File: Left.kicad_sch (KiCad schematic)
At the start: 193 parts, among them J1 USB_C_Receptacle_USB2.0, J2 USB_C_Receptacle_USB2.0, J3 AVR-ISP-6, Q1 DMN2041L, Q2 DMN2041L, SW1 RotaryEncoder, SW10 SW_Push, SW11 SW_Push, SW12 SW_Push, SW13 SW_Push, SW14 SW_Push, SW15 SW_Push, SW16 SW_Push, SW17 SW_Push, SW18 SW_Push, SW19 SW_Push, SW2 SW_Push, SW20 SW_Push, SW21 SW_Push, SW22 SW_Push, SW23 SW_Push, SW24 SW_Push, SW25 SW_Push, SW26 SW_Push, SW27 SW_Push, SW28 SW_Push, SW29 SW_Push, SW3 SW_Push, SW30 SW_Push, SW31 SW_Push, SW32 SW_Push, SW33 SW_Push, SW34 SW_Push, SW35 SW_Push, SW36 SW_Push, SW37 SW_Push, SW38 SW_Push, SW39 SW_Push, SW4 SW_Push, SW40 SW_Push, SW41 SW_Push, SW5 SW_Push, SW6 SW_Push, SW7 SW_Push, SW8 SW_Push, SW9 SW_Push, U1 ATmega32U4-A, Y1 16MHz

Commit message: replaced LEDs with RGBs, and started the PCB for keyboard
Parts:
- removed D10, D11, D12, D13, D14, D15, D16, D17, D18, D19, D2, D20, D21, D22, D23, D24, D25, D26, D27, D28, D29, D3, D30, D31, D32, D33, D34, D35, D36, D37, D38, D39, D4, D40, D41, D5, D6, D7, D8, D9: LED, symbol Device:LED
- removed D42, D47, D48, D54, D55, D62, D63, D69, D70, D76, D77: D_Small, symbol Device:D_Small
- removed Q1: DMN2041L, Package_TO_SOT_SMD:SOT-23, symbol Transistor_FET:DMN2041L
- removed R10, R11, R12, R13, R14, R15, R16, R17, R19, R20, R21, R24, R25, R26, R27, R28, R29, R3, R30, R31, R32, R33, R34, R35, R37, R38, R39, R4, R42, R43, R44, R45, R46, R47, R48, R5, R6, R7, R8, R9: 470, symbol Device:R_Small
- removed R49: 1k, symbol Device:R_Small
- removed SW14, SW15, SW2, SW21, SW22, SW28, SW29, SW35, SW36, SW7, SW8: SW_Push, keyswitches.pretty-2:Kailh_socket_PG1350, symbol Switch:SW_Push
- added C208, C209, C210, C211, C212, C213, C214, C215, C216, C217, C218, C219, C220, C221, C222, C223, C224, C225, C226, C227, C228, C229, C230, C231, C232, C233, C234, C235, C236, C237, C238, C239, C240, C241, C242, C243, C244, C245, C246, C247: 100nF, Capacitor_SMD:C_0402_1005Metric, symbol Device:C_Small
- added D203, D204, D205, D206, D207, D208, D209, D210, D211, D212, D213, D214, D215, D216, D217, D218, D219, D220, D221, D222, D223, D224, D225, D226, D227, D228, D229, D230, D231, D232, D233, D234, D235, D236, D237, D238, D239, D240, D241, D242: NeoPixel_THT, kicad-keyboard-parts.pretty:LED_RGB_Wuerth-PLCC4_3.2x2.8mm_150141M173100, symbol LED:NeoPixel_THT
- added D273, D274, D275, D276, D277, D278, D279, D280, D281, D282: D_Small, Diode_SMD:D_SOD-123, symbol Device:D_Small
- added FB201: FerriteBead_Small, Inductor_SMD:L_0805_2012Metric_Pad1.15x1.40mm_HandSolder, symbol Device:FerriteBead_Small
- added H201, H202, H203, H204, H205, H206: MountingHole, MountingHole:MountingHole_2.2mm_M2_DIN965_Pad, symbol Mechanical:MountingHole
- added R205: 300, Resistor_SMD:R_0402_1005Metric, symbol Device:R_Small
- added SW232, SW233, SW234, SW235, SW237, SW238, SW239, SW240, SW241: SW_Push, keyswitches.pretty-2:Kailh_socket_PG1350, symbol Switch:SW_Push
- added SW236: SW_Push, keyswitches.pretty-2:Kailh_socket_PG1350_2.25U, symbol Switch:SW_Push
- C201: renamed from C1; footprint (none) -> Capacitor_SMD:C_0402_1005Metric
- C202: renamed from C2; footprint (none) -> Capacitor_SMD:C_0402_1005Metric
- C203: renamed from C3; footprint (none) -> Capacitor_SMD:C_0402_1005Metric
- C204: renamed from C4; footprint (none) -> Capacitor_SMD:C_0402_1005Metric
- C205: renamed from C5; footprint (none) -> Capacitor_SMD:C_0402_1005Metric
- C206: renamed from C6; footprint (none) -> Capacitor_SMD:C_0402_1005Metric
- C207: renamed from C7; footprint (none) -> Capacitor_SMD:C_0402_1005Metric
- D243: renamed from D43; footprint (none) -> Diode_SMD:D_SOD-123
- D244: renamed from D44; footprint (none) -> Diode_SMD:D_SOD-123
- D245: renamed from D45; footprint (none) -> Diode_SMD:D_SOD-123
- D246: renamed from D46; footprint (none) -> Diode_SMD:D_SOD-123
- D247: renamed from D49; footprint (none) -> Diode_SMD:D_SOD-123
- D248: renamed from D50; footprint (none) -> Diode_SMD:D_SOD-123
- D249: renamed from D51; footprint (none) -> Diode_SMD:D_SOD-123
- D250: renamed from D52; footprint (none) -> Diode_SMD:D_SOD-123
- D251: renamed from D53; footprint (none) -> Diode_SMD:D_SOD-123
- D252: renamed from D56; footprint (none) -> Diode_SMD:D_SOD-123
- D253: renamed from D57; footprint (none) -> Diode_SMD:D_SOD-123
- D254: renamed from D58; footprint (none) -> Diode_SMD:D_SOD-123
- D255: renamed from D59; footprint (none) -> Diode_SMD:D_SOD-123
- D256: renamed from D60; footprint (none) -> Diode_SMD:D_SOD-123
- D257: renamed from D64; footprint (none) -> Diode_SMD:D_SOD-123
- D258: renamed from D65; footprint (none) -> Diode_SMD:D_SOD-123
- D259: renamed from D66; footprint (none) -> Diode_SMD:D_SOD-123
- D260: renamed from D67; footprint (none) -> Diode_SMD:D_SOD-123
- D261: renamed from D68; footprint (none) -> Diode_SMD:D_SOD-123
- D262: renamed from D61; footprint (none) -> LED_SMD:LED_PLCC_2835
- D263: renamed from D71; footprint (none) -> Diode_SMD:D_SOD-123
- D264: renamed from D72; footprint (none) -> Diode_SMD:D_SOD-123
- D265: renamed from D73; footprint (none) -> Diode_SMD:D_SOD-123
- D266: renamed from D74; footprint (none) -> Diode_SMD:D_SOD-123
- D267: renamed from D75; footprint (none) -> Diode_SMD:D_SOD-123
- D268: renamed from D78; footprint (none) -> Diode_SMD:D_SOD-123
- D269: renamed from D79; footprint (none) -> Diode_SMD:D_SOD-123
- D270: renamed from D80; footprint (none) -> Diode_SMD:D_SOD-123
- D271: renamed from D81; footprint (none) -> Diode_SMD:D_SOD-123
- D272: renamed from D82; footprint (none) -> Diode_SMD:D_SOD-123
- F201: renamed from F1; footprint (none) -> Keebio-Parts:Fuse_0805
- J201: renamed from J2; footprint (none) -> Type-C:HRO-TYPE-C-31-M-13
- J202: renamed from J1; footprint (none) -> Type-C:HRO-TYPE-C-31-M-13
- J203: renamed from J3; footprint (none) -> Keebio-Parts:ICSP-Header
- R201: renamed from R1; footprint (none) -> Resistor_SMD:R_0402_1005Metric
- R202: renamed from R52; footprint (none) -> Resistor_SMD:R_0402_1005Metric
- R203: renamed from R2; footprint (none) -> Resistor_SMD:R_0402_1005Metric
- R204: renamed from R53; footprint (none) -> Resistor_SMD:R_0402_1005Metric
- R220: renamed from R18; footprint (none) -> Resistor_SMD:R_0402_1005Metric
- R224: renamed from R22; footprint (none) -> Resistor_SMD:R_0402_1005Metric
- R225: renamed from R23; footprint (none) -> Resistor_SMD:R_0402_1005Metric
- R238: renamed from R36; footprint (none) -> Resistor_SMD:R_0402_1005Metric
- R242: renamed from R40; footprint (none) -> Resistor_SMD:R_0402_1005Metric
- R243: renamed from R41; footprint (none) -> Resistor_SMD:R_0402_1005Metric
- R252: renamed from R50; footprint (none) -> Resistor_SMD:R_0402_1005Metric
- R253: renamed from R51; footprint (none) -> Resistor_SMD:R_0402_1005Metric
- SW202: renamed from SW1; footprint (none) -> Rotary_Encoder.pretty:kailh_EN97xx_rotary_encoder
- SW213: renamed from SW17; footprint keyswitches.pretty-2:Kailh_socket_PG1350 -> keyswitches.pretty-2:Kailh_socket_PG1350_1.5U
- SW214: renamed from SW18; footprint keyswitches.pretty-2:Kailh_socket_PG1350 -> keyswitches.pretty-2:Kailh_socket_PG1350_1.75U
- SW215: renamed from SW19; footprint keyswitches.pretty-2:Kailh_socket_PG1350 -> keyswitches.pretty-2:Kailh_socket_PG1350_2.25U
- SW216: renamed from SW20; footprint keyswitches.pretty-2:Kailh_socket_PG1350 -> keyswitches.pretty-2:Kailh_socket_PG1350_1.25U
- SW221: renamed from SW27; footprint keyswitches.pretty-2:Kailh_socket_PG1350 -> keyswitches.pretty-2:Kailh_socket_PG1350_1.25U
- SW226: renamed from SW34; footprint keyswitches.pretty-2:Kailh_socket_PG1350 -> keyswitches.pretty-2:Kailh_socket_PG1350_1.25U
- SW231: renamed from SW41; footprint keyswitches.pretty-2:Kailh_socket_PG1350 -> keyswitches.pretty-2:Kailh_socket_PG1350_1.25U
- Y201: renamed from Y1; footprint (none) -> Crystal:Crystal_SMD_3225-4Pin_3.2x2.5mm
- gave numbers to parts that had none: 1
- renumbered D1 to D201, Q2 to Q202, SW_RESET1 to SW201, SW3 to SW203, SW4 to SW204, SW5 to SW205, SW6 to SW206, SW9 to SW207, SW10 to SW208, SW11 to SW209, SW12 to SW210, SW13 to SW211, SW16 to SW212, SW23 to SW217, SW24 to SW218, SW25 to SW219, SW26 to SW220, SW30 to SW222, SW31 to SW223, SW32 to SW224, SW33 to SW225, SW37 to SW227, SW38 to SW228, SW39 to SW229, SW40 to SW230, U1 to U201
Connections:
- net +5V: now also C208.2, C209.2, C210.2, C211.2, C212.1, C212.2, C213.2, C214.2, C215.2, C216.2, C217.2, C218.2, C219.2, C220.2, C221.2, C222.2, C223.2, C224.2, C225.2, C226.2, C227.2, C228.2, C229.2, C230.2, C231.2, C232.2, C233.2, C234.2, C235.2, C236.2, C237.2, C238.2, C239.2, C240.2, C241.2, C242.2, C243.2, C244.2, C245.2, C246.2, C247.1, C247.2, D203.3 (VDD), D204.3 (VDD), D205.3 (VDD), D206.3 (VDD), D207.3 (VDD), D208.3 (VDD), D209.3 (VDD), D210.3 (VDD), D211.3 (VDD), D212.3 (VDD), D213.3 (VDD), D214.3 (VDD), D215.3 (VDD), D216.3 (VDD), D217.3 (VDD), D218.3 (VDD), D219.3 (VDD), D220.3 (VDD), D221.3 (VDD), D222.3 (VDD), D223.3 (VDD), D224.3 (VDD), D225.3 (VDD), D226.3 (VDD), D227.3 (VDD), D228.3 (VDD), D229.3 (VDD), D230.3 (VDD), D231.3 (VDD), D232.3 (VDD), D233.3 (VDD), D234.2 (GND), D234.3 (VDD), D235.3 (VDD), D236.3 (VDD), D237.3 (VDD), D238.3 (VDD), D239.3 (VDD), D240.3 (VDD), D241.3 (VDD), D242.3 (VDD)
- net GND: now also C208.1, C209.1, C210.1, C211.1, C213.1, C214.1, C215.1, C216.1, C217.1, C218.1, C219.1, C220.1, C221.1, C222.1, C223.1, C224.1, C225.1, C226.1, C227.1, C228.1, C229.1, C230.1, C231.1, C232.1, C233.1, C234.1, C235.1, C236.1, C237.1, C238.1, C239.1, C240.1, C241.1, C242.1, C243.1, C244.1, C245.1, C246.1, D203.2 (GND), D204.2 (GND), D205.2 (GND), D206.2 (GND), D207.2 (GND), D208.2 (GND), D209.2 (GND), D210.2 (GND), D211.2 (GND), D212.2 (GND), D213.2 (GND), D214.2 (GND), D215.2 (GND), D216.2 (GND), D217.2 (GND), D218.2 (GND), D219.2 (GND), D220.2 (GND), D221.2 (GND), D222.2 (GND), D223.2 (GND), D224.2 (GND), D225.2 (GND), D226.2 (GND), D227.2 (GND), D228.2 (GND), D229.2 (GND), D230.2 (GND), D231.2 (GND), D232.2 (GND), D233.2 (GND), D235.2 (GND), D236.2 (GND), D237.2 (GND), D238.2 (GND), D239.2 (GND), D240.2 (GND), D241.2 (GND), D242.2 (GND), FB201.2; no longer J201.S1 (SHIELD)
- net ROW_0: now also D277.1 (K), D282.1 (K)
- net ROW_1: now also D276.1 (K), D281.1 (K)
- net ROW_2: now also D275.1 (K), D280.1 (K)
- net ROW_3: now also D274.1 (K), D279.1 (K)
- net ROW_4: now also D273.1 (K), D278.1 (K)
- net D_P: now reaches R224.2, U201.4 (D+)
- net D_N: now reaches R220.2, U201.3 (D-)
- net PWM: no longer names the net of U201.12 (PB7)
- net PWM: now also R205.1
- net ROW_5 renamed COL_6
- net COL_6: now also SW232.2, SW233.2, SW234.2, SW235.2, SW236.2
- net ROW_6 renamed COL_7
- net COL_7: now also SW237.2, SW238.2, SW239.2, SW240.2, SW241.2
- new net: D282.2 (A), SW241.1
- new net: D229.1 (DOUT), D230.4 (DIN)
- new net: D228.1 (DOUT), D229.4 (DIN)
- new net: D275.2 (A), SW234.1
- new net: D281.2 (A), SW240.1
- new net: D273.2 (A), SW232.1
- new net: D213.1 (DOUT), D214.4 (DIN)
- new net: D212.1 (DOUT), D213.4 (DIN)
- new net: D230.1 (DOUT), D231.4 (DIN)
- new net: D209.1 (DOUT), D210.4 (DIN)
- new net: D235.1 (DOUT), D236.4 (DIN)
- new net: D222.1 (DOUT), D223.4 (DIN)
- new net: D221.1 (DOUT), D222.4 (DIN)
- new net: D206.1 (DOUT), D207.4 (DIN)
- new net: D205.1 (DOUT), D206.4 (DIN)
- new net: D236.1 (DOUT), D237.4 (DIN)
- new net: D225.1 (DOUT), D226.4 (DIN)
- new net: D224.1 (DOUT), D225.4 (DIN)
- new net: D239.1 (DOUT), D240.4 (DIN)
- new net: D238.1 (DOUT), D239.4 (DIN)
- new net: D217.1 (DOUT), D218.4 (DIN)
- new net: D216.1 (DOUT), D217.4 (DIN)
- new net: D237.1 (DOUT), D238.4 (DIN)
- new net: D241.1 (DOUT), D242.4 (DIN)
- new net: D240.1 (DOUT), D241.4 (DIN)
- new net: D278.2 (A), SW237.1
- new net: D227.1 (DOUT), D228.4 (DIN)
- new net: D219.1 (DOUT), D220.4 (DIN)
- new net: D204.1 (DOUT), D205.4 (DIN)
- new net: D211.1 (DOUT), D212.4 (DIN)
- new net: D279.2 (A), SW238.1
- new net: D274.2 (A), SW233.1
- new net: D203.1 (DOUT), D204.4 (DIN)
- new net: D220.1 (DOUT), D221.4 (DIN)
- new net: D280.2 (A), SW239.1
- new net: D215.1 (DOUT), D216.4 (DIN)
- new net: D208.1 (DOUT), D209.4 (DIN)
- new net: D276.2 (A), SW235.1
- new net: D207.1 (DOUT), D208.4 (DIN)
- new net: D231.1 (DOUT), D232.4 (DIN)
- new net: D277.2 (A), SW236.1
- new net: D233.1 (DOUT), D234.4 (DIN)
- new net: D232.1 (DOUT), D233.4 (DIN)
- new net: D214.1 (DOUT), D215.4 (DIN)
- new net: D223.1 (DOUT), D224.4 (DIN)
- new net D211: D210.1 (DOUT), D211.4 (DIN)
- new net D219: D218.1 (DOUT), D219.4 (DIN)
- new net D227: D226.1 (DOUT), D227.4 (DIN)
- new net D235: D234.1 (DOUT), D235.4 (DIN)
- new net Earth: FB201.1, J201.S1 (SHIELD)
- new net RGB: D203.4 (DIN), R205.2
- no-connect marks 8 -> 9
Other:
- note added: "39 switch matrix"
- note added: "40 RGB LEDs Matrix"
- note removed: "40 LEDs"
- note removed: "40 switch matrix"
- moved on the sheet: C203, D201, D202, D243, D244, D245, D246, D247, D248, D249, D250, D251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

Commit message: did some more work on the keyboard, played around with the rotary footprint
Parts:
- SW201: footprint Button_Switch_SMD:SW_SPST_SKQG_WithStem -> Keebio-Parts:SW_SPST_TL3342
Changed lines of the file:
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@@
     (property "Reference" "SW201" (id 0) (at 190.5 77.47 0))
     (property "Value" "SW_Push" (id 1) (at 190.5 80.01 0))
-    (property "Footprint" "Button_Switch_SMD:SW_SPST_SKQG_WithStem" (id 2) (at 190.5 80.01 0)
+    (property "Footprint" "Keebio-Parts:SW_SPST_TL3342" (id 2) (at 190.5 80.01 0)
       (effects (font (size 1.27 1.27)) hide)
     )

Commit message: did some routing
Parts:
- removed D202: PRTR5V0U2X, Package_TO_SOT_SMD:SOT-143, symbol Power_Protection:PRTR5V0U2X
- removed D262: LED, LED_SMD:LED_PLCC_2835, symbol Device:LED
- removed J202: USB_C_Receptacle_USB2.0, Type-C:HRO-TYPE-C-31-M-13, symbol Connector:USB_C_Receptacle_USB2.0
- removed Q202: DMN2041L, Package_TO_SOT_SMD:SOT-23, symbol Transistor_FET:DMN2041L
- removed R202, R204: 5.1k, Resistor_SMD:R_0402_1005Metric, symbol Device:R_Small
- removed R252: 470, Resistor_SMD:R_0402_1005Metric, symbol Device:R_Small
- removed R253: 1k, Resistor_SMD:R_0402_1005Metric, symbol Device:R_Small
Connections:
- net +5V: now also R242.1, R243.1
- net DATA_1: now also U201.20 (PD2)
- net DATA_2: now also U201.21 (PD3)
- no-connect marks 9 -> 7
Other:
- note removed: "CAPS LOCK LED"
- moved on the sheet: R242, R243

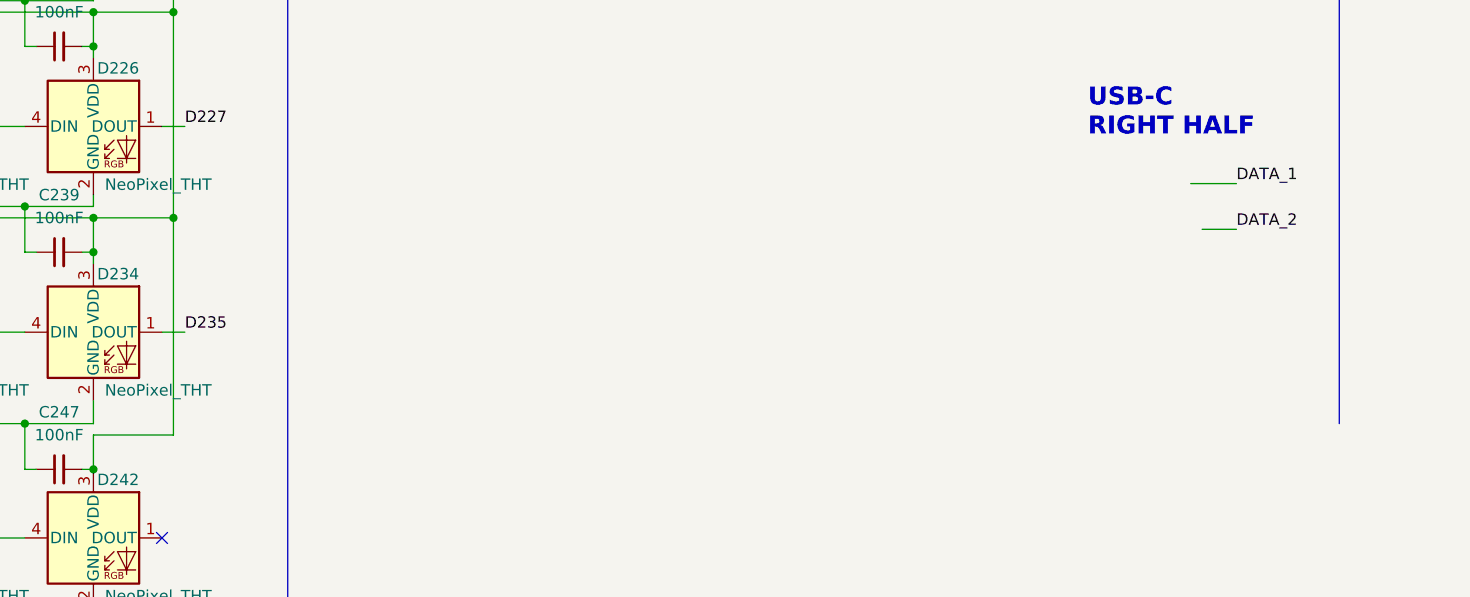
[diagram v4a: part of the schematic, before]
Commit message: placed some i2cs
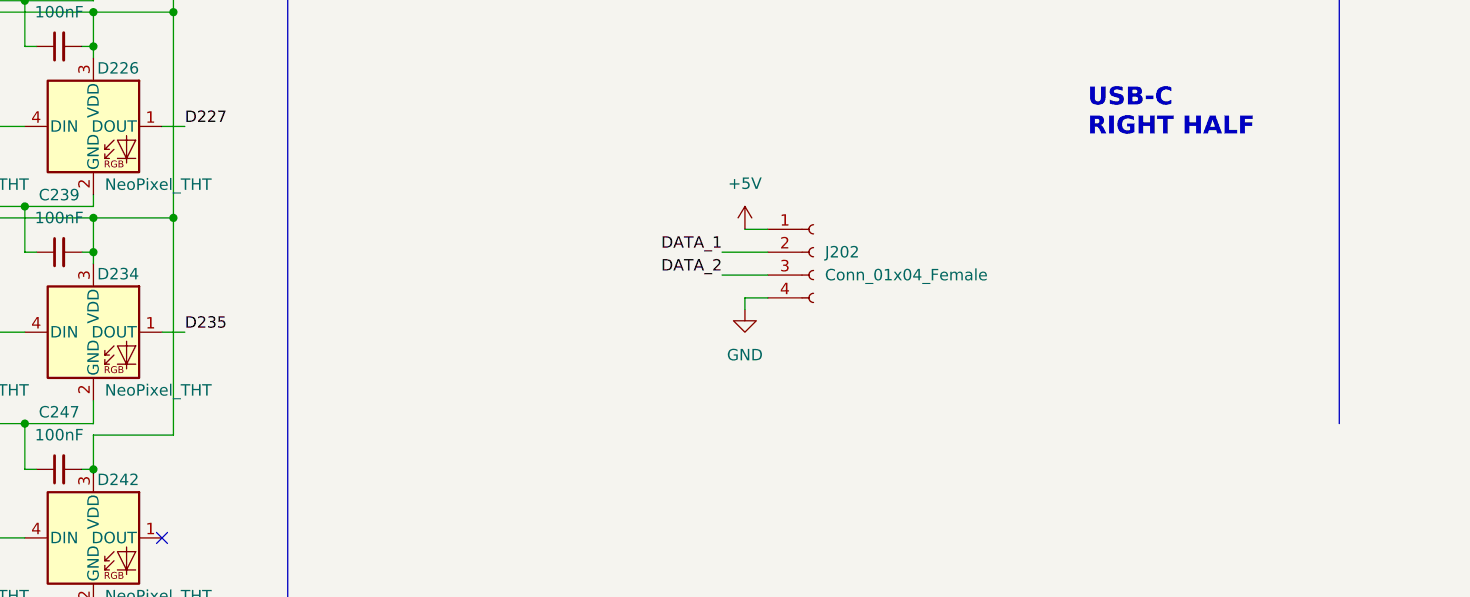
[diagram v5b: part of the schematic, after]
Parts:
- added J202: Conn_01x04_Female, Keebio-Parts:I2C_Breakout, symbol Connector:Conn_01x04_Female
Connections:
- net +5V: now also J202.1 (Pin_1)
- net DATA_1: now also J202.2 (Pin_2)
- net DATA_2: now also J202.3 (Pin_3)
- net GND: now also J202.4 (Pin_4)
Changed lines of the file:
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@@
     (stroke (width 0) (type default) (color 0 0 0 0))
   )
+  (wire (pts (xy 246.38 220.98) (xy 246.38 222.25))
+    (stroke (width 0) (type default) (color 0 0 0 0))
+  )
   (wire (pts (xy 86.36 39.37) (xy 86.36 45.72))
     (stroke (width 0) (type default) (color 0 0 0 0))
@@
     (stroke (width 0) (type default) (color 0 0 0 0))
   )
-  (wire (pts (xy 182.88 236.22) (xy 182.88 212.09))
-    (stroke (width 0) (type default) (color 0 0 0 0))
-  )
   (wire (pts (xy 52.07 212.09) (xy 72.39 212.09))
     (stroke (width 0) (type default) (color 0 0 0 0))
@@
     (stroke (width 0) (type default) (color 0 0 0 0))
   )
-  (wire (pts (xy 300.99 213.36) (xy 297.18 213.36))
+  (wire (pts (xy 243.84 218.44) (xy 248.92 218.44))
     (stroke (width 0) (type default) (color 0 0 0 0))
   )
@@
     (stroke (width 0) (type default) (color 0 0 0 0))
   )
-  (wire (pts (xy 181.61 224.79) (xy 184.15 224.79))
-    (stroke (width 0) (type default) (color 0 0 0 0))
-  )
   (wire (pts (xy 52.07 166.37) (xy 52.07 170.18))
     (stroke (width 0) (type default) (color 0 0 0 0))
@@
     (stroke (width 0) (type default) (color 0 0 0 0))
   )
+  (wire (pts (xy 246.38 220.98) (xy 248.92 220.98))
+    (stroke (width 0) (type default) (color 0 0 0 0))
+  )
   (wire (pts (xy 248.92 118.11) (xy 248.92 123.19))
     (stroke (width 0) (type default) (color 0 0 0 0))
@@
     (stroke (width 0) (type default) (color 0 0 0 0))
   )
-  (wire (pts (xy 300.99 208.28) (xy 295.91 208.28))
-    (stroke (width 0) (type default) (color 0 0 0 0))
-  )
   (wire (pts (xy 299.72 120.65) (xy 299.72 121.92))
     (stroke (width 0) (type default) (color 0 0 0 0))
@@
     (stroke (width 0) (type default) (color 0 0 0 0))
   )
+  (wire (pts (xy 184.15 224.79) (xy 181.61 224.79))
+    (stroke (width 0) (type default) (color 0 0 0 0))
+  )
   (wire (pts (xy 39.37 247.65) (xy 44.45 247.65))
     (stroke (width 0) (type default) (color 0 0 0 0))
@@
     (stroke (width 0) (type default) (color 0 0 0 0))
   )
+  (wire (pts (xy 246.38 213.36) (xy 248.92 213.36))
+    (stroke (width 0) (type default) (color 0 0 0 0))
+  )
   (wire (pts (xy 173.99 232.41) (xy 173.99 234.95))
     (stroke (width 0) (type default) (color 0 0 0 0))
@@
     (stroke (width 0) (type default) (color 0 0 0 0))
   )
+  (wire (pts (xy 243.84 215.9) (xy 248.92 215.9))
+    (stroke (width 0) (type default) (color 0 0 0 0))
+  )
   (wire (pts (xy 82.55 39.37) (xy 82.55 63.5))
     (stroke (width 0) (type default) (color 0 0 0 0))
@@
     (stroke (width 0) (type default) (color 0 0 0 0))
   )
+  (wire (pts (xy 182.88 212.09) (xy 182.88 236.22))
+    (stroke (width 0) (type default) (color 0 0 0 0))
+  )
   (wire (pts (xy 309.88 135.89) (xy 311.15 135.89))
     (stroke (width 0) (type default) (color 0 0 0 0))
@@
     (effects (font (size 1.27 1.27)) (justify left bottom))
   )
-  (label "DATA_2" (at 300.99 213.36 0)
-    (effects (font (size 1.27 1.27)) (justify left bottom))
+  (label "DATA_2" (at 243.84 218.44 180)
+    (effects (font (size 1.27 1.27)) (justify right bottom))
   )
   (label "RST" (at 194.31 40.64 0)
@@
     (effects (font (size 1.27 1.27)) (justify right bottom))
   )
-  (label "DATA_1" (at 300.99 208.28 0)
-    (effects (font (size 1.27 1.27)) (justify left bottom))
+  (label "DATA_1" (at 243.84 215.9 180)
+    (effects (font (size 1.27 1.27)) (justify right bottom))
   )
   (label "D-" (at 180.34 113.03 180)
@@
     (pin "4")
   )
+  (symbol (lib_id "power:GND") (at 246.38 222.25 0) (unit 1)
+    (in_bom yes) (on_board yes) (fields_autoplaced)
+    (property "Reference" "#PWR0204" (id 0) (at 246.38 228.6 0)
+      (effects (font (size 1.27 1.27)) hide)
+    )
+    (property "Value" "GND" (id 1) (at 246.38 227.33 0))
+    (property "Footprint" "" (id 2) (at 246.38 222.25 0)
+      (effects (font (size 1.27 1.27)) hide)
+    )
+    (property "Datasheet" "" (id 3) (at 246.38 222.25 0)
+      (effects (font (size 1.27 1.27)) hide)
+    )
+    (pin "1")
+  )
   (symbol (lib_id "Device:C_Small") (at 220.98 31.75 0) (unit 1)
     (in_bom yes) (on_board yes) (fields_autoplaced)
@@
     (pin "2")
   )
+  (symbol (lib_id "power:+5V") (at 246.38 213.36 0) (unit 1)
+    (in_bom yes) (on_board yes) (fields_autoplaced)
+    (property "Reference" "#PWR0202" (id 0) (at 246.38 217.17 0)
+      (effects (font (size 1.27 1.27)) hide)
+    )
+    (property "Value" "+5V" (id 1) (at 246.38 208.28 0))
+    (property "Footprint" "" (id 2) (at 246.38 213.36 0)
+      (effects (font (size 1.27 1.27)) hide)
+    )
+    (property "Datasheet" "" (id 3) (at 246.38 213.36 0)
+      (effects (font (size 1.27 1.27)) hide)
+    )
+    (pin "1")
+  )
   (symbol (lib_id "Device:D_Small") (at 332.74 118.11 90) (unit 1)
     (in_bom yes) (on_board yes)
@@
   (symbol (lib_id "power:+5V") (at 255.27 110.49 0) (unit 1)
     (in_bom yes) (on_board yes) (fields_autoplaced)
-    (property "Reference" "#PWR?" (id 0) (at 255.27 114.3 0)
+    (property "Reference" "#PWR0103" (id 0) (at 255.27 114.3 0)
       (effects (font (size 1.27 1.27)) hide)
     )
@@
     )
     (pin "1")
+    (pin "2")
+    (pin "3")
+    (pin "4")
+  )
+  (symbol (lib_id "Connector:Conn_01x04_Female") (at 254 215.9 0) (unit 1)
+    (in_bom yes) (on_board yes) (fields_autoplaced)
+    (property "Reference" "J202" (id 0) (at 255.27 215.8999 0)
+      (effects (font (size 1.27 1.27)) (justify left))
+    )
+    (property "Value" "Conn_01x04_Female" (id 1) (at 255.27 218.4399 0)
+      (effects (font (size 1.27 1.27)) (justify left))
+    )
+    (property "Footprint" "Keebio-Parts:I2C_Breakout" (id 2) (at 254 215.9 0)
+      (effects (font (size 1.27 1.27)) hide)
+    )
+    (property "Datasheet" "~" (id 3) (at 254 215.9 0)
+      (effects (font (size 1.27 1.27)) hide)
+    )
+    (pin "1")
